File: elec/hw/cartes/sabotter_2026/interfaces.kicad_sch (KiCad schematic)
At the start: 43 parts, among them J10 2-1445055-3, J11 3-794618-6, J12 22053031, J13 3-794618-6, J6 794618-4, J7 A3C-16DA-2DSC71, J8 A3C-16DA-2DSC71, J9 794618-4, U6 TCAN1042DRQ1, U7 TCA6408ARGTR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

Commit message: switchs added to motor ribbon cable
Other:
- moved on the sheet: C27, D6, R51, R52, R53, R58, TP6, U7

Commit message: sabotter wip
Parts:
- removed J10: 2-1445055-3, cocotter_connectors:2-1445055-3, symbol cocotter_connectors:2-1445055-3
- removed J11: 3-794618-6, cocotter_connectors:3-794618-6, symbol cocotter_connectors:3-794618-6
- removed J12: 22053031, cocotter_connectors:22053031, symbol cocotter_connectors:22053031
- removed J7: A3C-16DA-2DSC71, cocotter_connectors:A3C-16DA-2DSC71, symbol cocotter_connectors:sabotter_to_unioc_pw
- removed J8: A3C-16DA-2DSC71, cocotter_connectors:A3C-16DA-2DSC71, symbol cocotter_connectors:sabotter_to_unioc_com
- removed R57: 91k 1%, cocotter_resistor:r0603_reflow, symbol cocotter_resistors:R_91k_0603_1%
- added C30: 100nF 50V, cocotter_capacitors:C_0603_1608Metric, symbol cocotter_capacitors:C_100nF_50V_0603
- added J10: 2-1445051-3, cocotter_connectors:2-1445051-3, symbol cocotter_connectors:2-1445051-3
- added J11: 22272051, cocotter_connectors:22272051, symbol cocotter_connectors:22272051
- added J12: 22272031, cocotter_connectors:22272031, symbol cocotter_connectors:22272031
- added J18: ~, cocotter_connectors:188275-4, symbol cocotter_connectors:unioc_uart
- added R58, R59, R60, R61: 0R, cocotter_resistor:r0603_reflow, symbol cocotter_resistors:R_0R_0603
- added R62, R63: 91k 1%, cocotter_resistor:r0603_reflow, symbol cocotter_resistors:R_91k_0603_1%
- added U9: ~, cocotter_ic:OLED_0.96inch, symbol cocotter_ic:OLED_0.96inch
- J13: value 3-794618-6 -> 3-794630-6; footprint cocotter_connectors:3-794618-6 -> cocotter_connectors:3-794630-6; symbol cocotter_connectors:3-794618-6 -> cocotter_connectors:3-794630-6
- J6, J9: value 794618-4 -> 3-794630-4; footprint cocotter_connectors:798618-4 -> cocotter_connectors:3-794630-4; symbol cocotter_connectors:794618-4 -> cocotter_connectors:3-794630-4
- renumbered R51 to R50, R50 to R51, R56 to R54, R54 to R55, R55 to R56, R58 to R57
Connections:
- net +3V3: now also J13.4, J11.4, R60.2, R61.2; no longer J13.2
- net +5V: now also J12.3
- net CAN_H: now also J10.3
- net CAN_L: now also J10.2
- net GND: now also C30.2, J10.1, J11.1, J12.1, J18.2 (GND), R58.1, R59.2, R62.2, R63.2
- net brake_mot_3v3: now also U7.7 (P4); no longer U7.9 (P6)
- net can_tx_3v3: now also U6.1 (TXD); no longer U6.3 (Vcc)
- net ctc_left_3v3: now also U7.8 (P5); no longer U7.5 (P3)
- net ctc_right_3v3: now also U7.9 (P6); no longer U7.4 (P2)
- net enable_tof_3v3: now also J13.5, U7.4 (P2), R63.1; no longer J13.4, U7.8 (P5)
- net reset_tof_3v3: now also U7.5 (P3), R62.1; no longer U7.7 (P4)
- net scl_3v3: now also J11.2, U9.3 (SCL)
- net scl_tof_3v3: now also J13.2; no longer J13.3
- net sda_3v3: now also J11.3, U9.4 (SDA)
- net sda_tof_3v3: now also J13.3; no longer J13.5
- net at D7.2 (DOUT): now also J12.2
- net at R54.2: now also J11.5
- net at R45.1: now also J18.1 (RX_from_out)
- net at R43.1: now also J18.4 (TX_from_out)
- new net: C30.1, R59.1, R60.1, U9.2 (VCC)
- new net: R58.2, R61.1, U9.1 (GND)
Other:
- note added: "HMI screen"
- moved on the sheet: R54

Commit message: sabotter wip
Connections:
- net brake_mot_3v3: now also U7.5 (P3); no longer U7.7 (P4)
- net color_select_3v3: now also U7.10 (P7); no longer U7.3 (P1)
- net ctc_left_3v3: now also U7.7 (P4); no longer U7.8 (P5)
- net ctc_right_3v3: now also U7.8 (P5); no longer U7.9 (P6)
- net enable_tof_3v3: now also U7.3 (P1); no longer U7.4 (P2)
- net led_com_3v3: now also U7.2 (P0); no longer U7.10 (P7)
- net reset_tof_3v3: now also U7.4 (P2); no longer U7.5 (P3)
- net scl_tof_3v3: now also J13.3; no longer J13.2
- net sda_tof_3v3: now also J13.2; no longer J13.3
- net starting_cord_3v3: now also U7.9 (P6); no longer U7.2 (P0)
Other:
- moved on the sheet: D6, R57, TP6

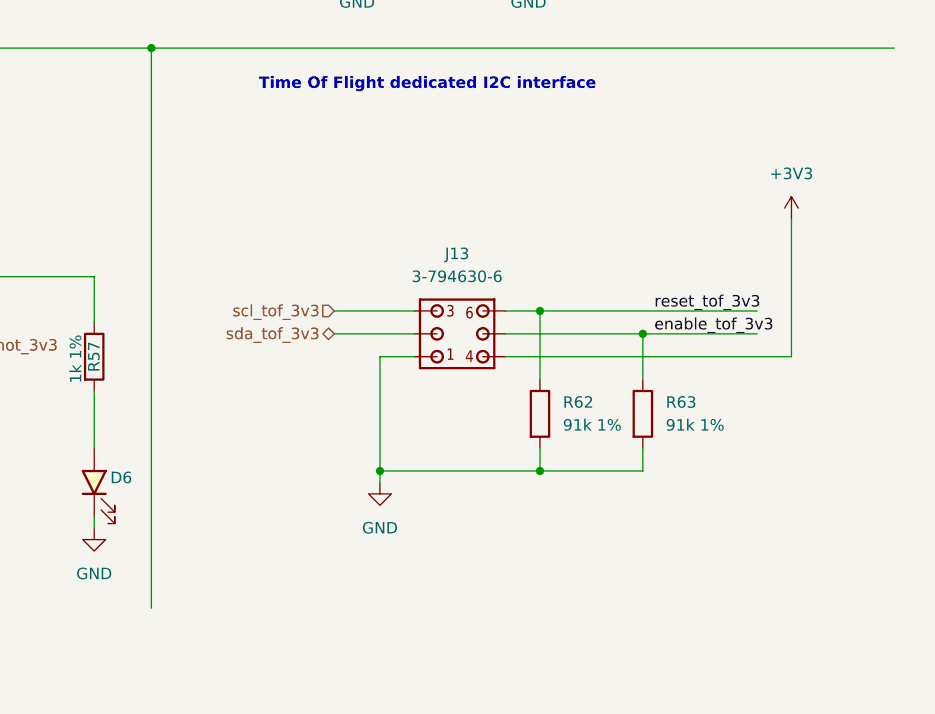
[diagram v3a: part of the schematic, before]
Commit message: tof irq added, needs routing
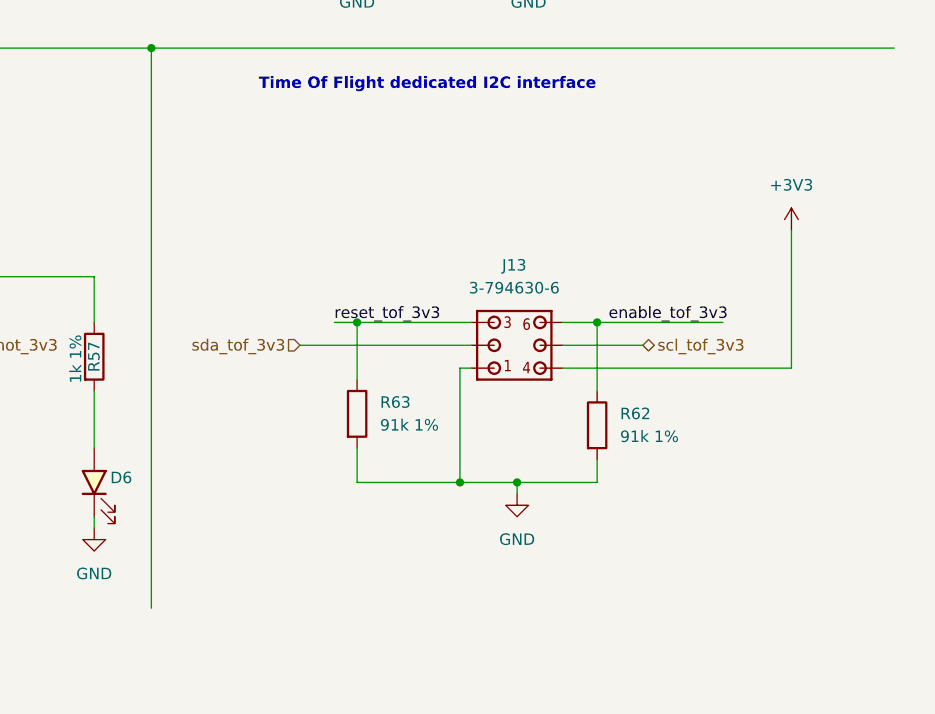
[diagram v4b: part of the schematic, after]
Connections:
- net enable_tof_3v3: now also J13.6, R62.1; no longer J13.5, R63.1
- net reset_tof_3v3: now also J13.3, R63.1; no longer J13.6, R62.1
- net scl_tof_3v3: now also J13.5; no longer J13.3
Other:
- moved on the sheet: J13, R62, R63

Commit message: sabotter corrections wip
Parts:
- added R65: 0R, cocotter_resistor:r0603_reflow, symbol cocotter_resistors:R_0R_0603
- added SW3: SLW-713515-2A-SMT-TR, cocotter_others:SLW-713515-2A-SMT-TR, symbol cocotter_connectors:SLW-713515-2A-SMT-TR
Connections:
- net GND: now also SW3.2
- net color_select_3v3: now also R65.2
- new net: R65.1, SW3.1
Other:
- moved on the sheet: C25, C26, C27, D6, J9, R49, R50, R51, R52, R53, R57, TP6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

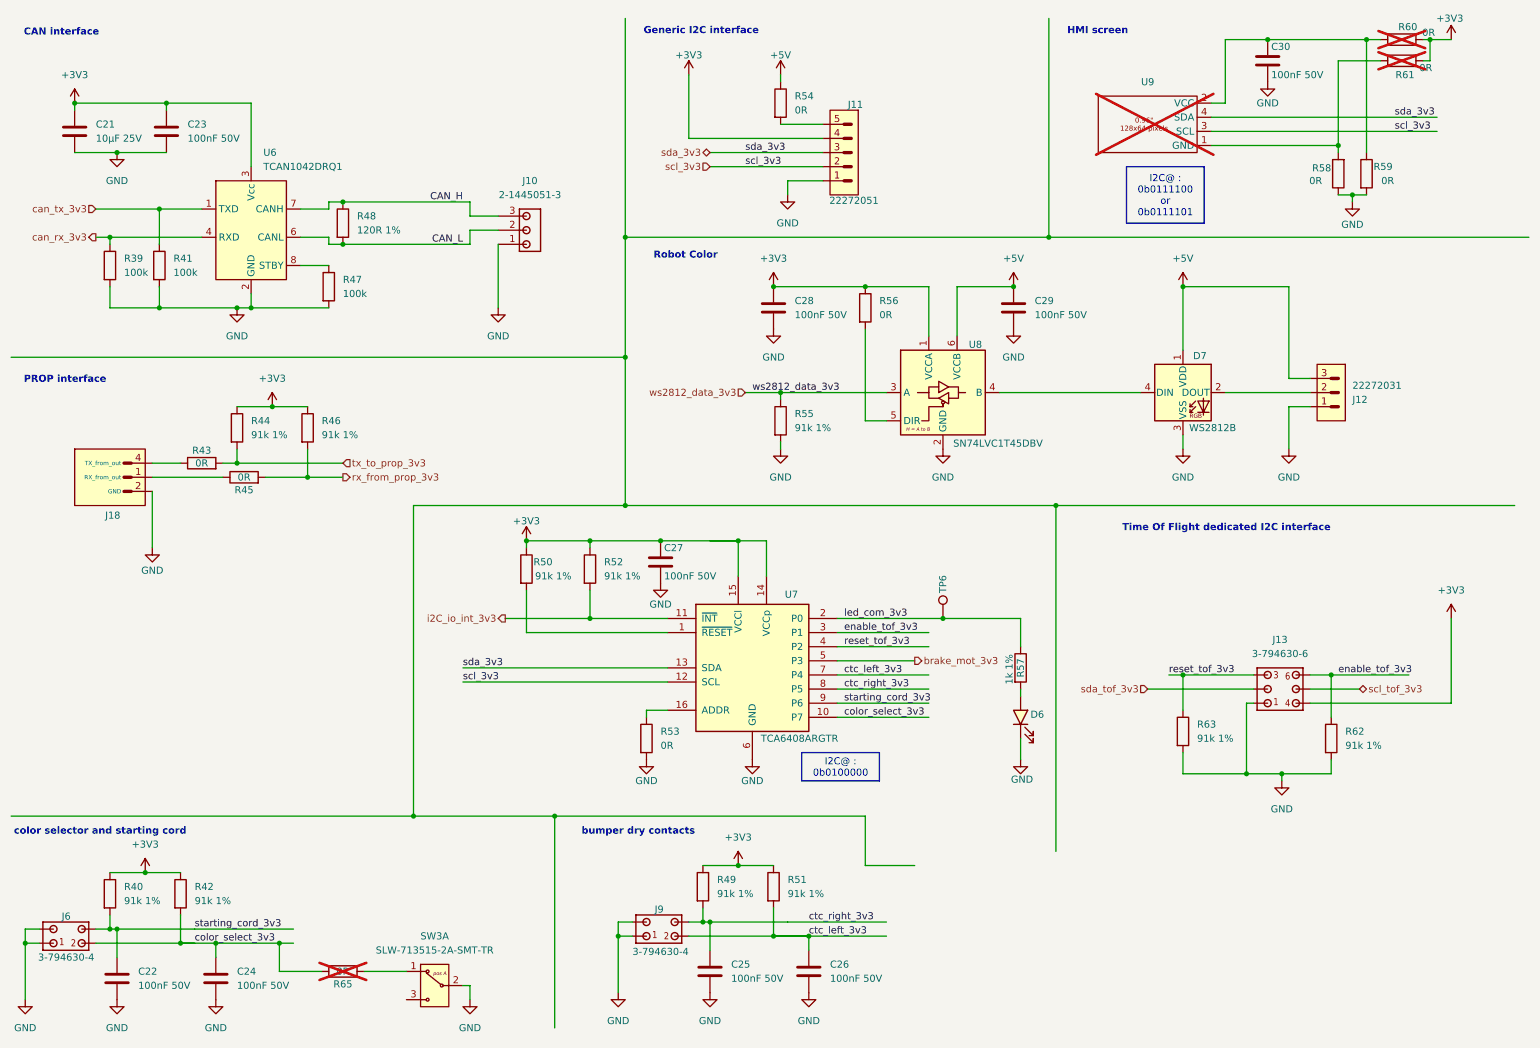
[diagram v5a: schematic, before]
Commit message: sabotter upodate : switch added to uc reset and color selection
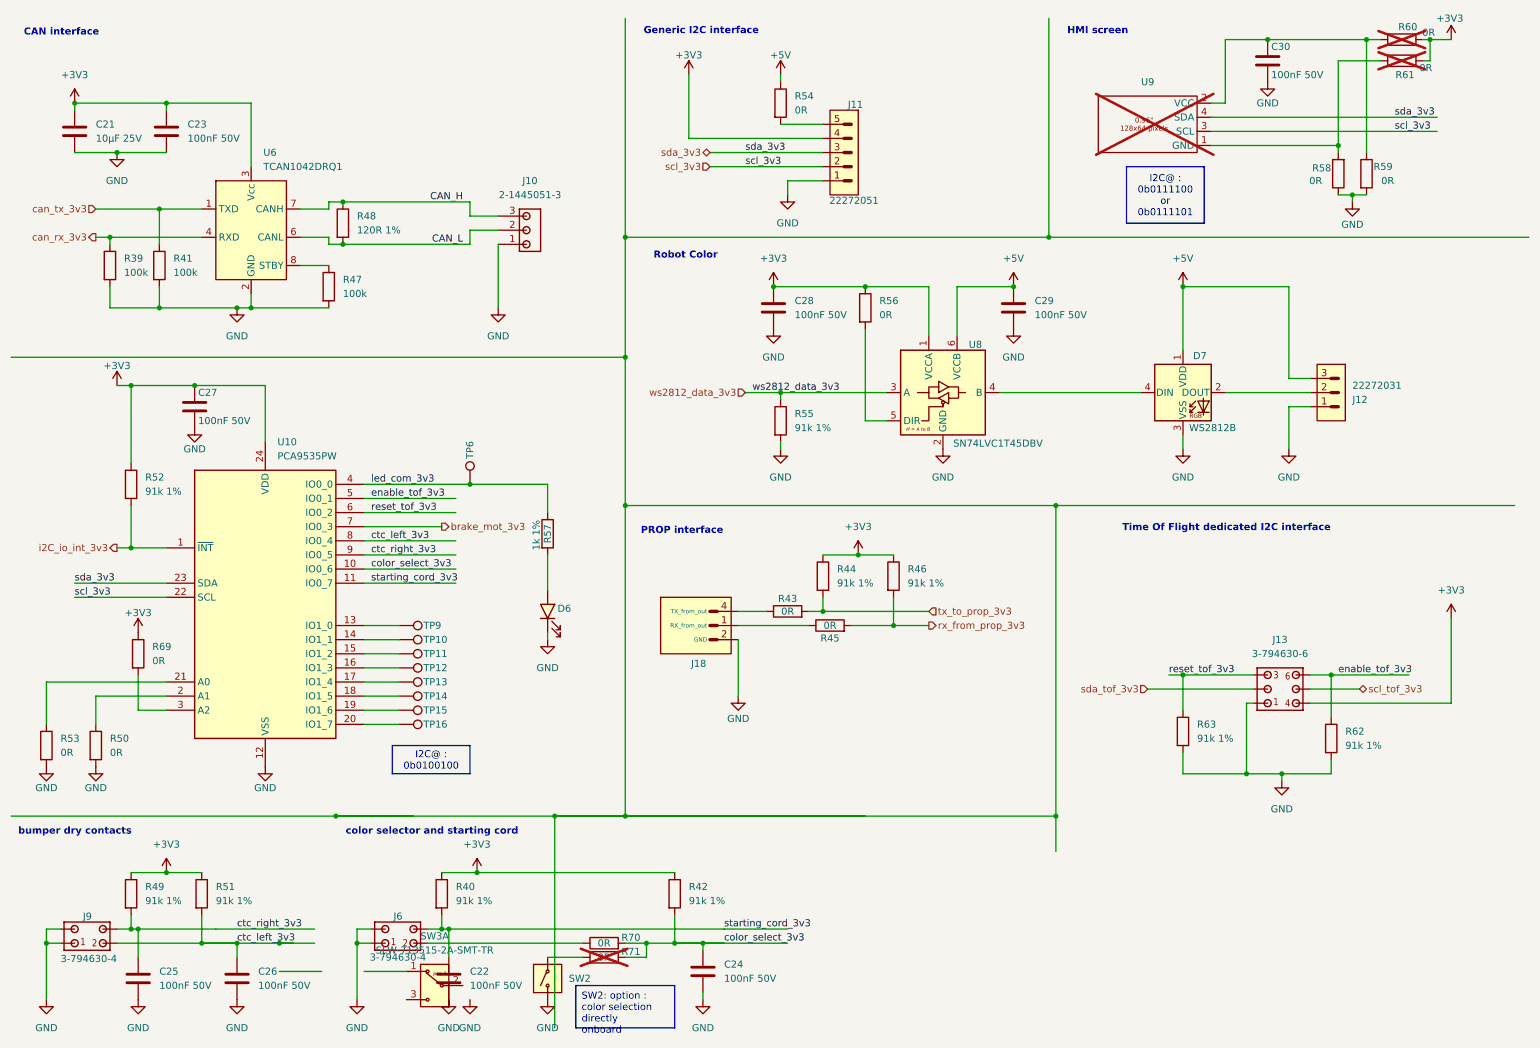
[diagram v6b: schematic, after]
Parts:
- removed R50: 91k 1%, cocotter_resistor:r0603_reflow, symbol cocotter_resistors:R_91k_0603_1%
- removed R65: 0R, cocotter_resistor:r0603_reflow, symbol cocotter_resistors:R_0R_0603
- removed U7: TCA6408ARGTR, cocotter_ic:VQFN-16-1EP_3x3mm_P0.5mm_EP1.1x1.1mm, symbol cocotter_ic:TCA6408ARGTR
- added R50, R69, R70, R71: 0R, cocotter_resistor:r0603_reflow, symbol cocotter_resistors:R_0R_0603
- added SW2: DSIC01LSGER, cocotter_others:DIP_SW_SMD-1P, symbol cocotter_others:DIP_SW_SMD-1P
- added TP10, TP11, TP12, TP13, TP14, TP15, TP16, TP9: TestPoint, cocotter_others:testpoint-THT-0.5mm, symbol cocotter_others:TestPoint
- added U10: PCA9535PW, Package_SO:TSSOP-24_4.4x7.8mm_P0.65mm, symbol cocotter_ic:PCA9535PW
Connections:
- net +3V3: now also R69.1, U10.24 (VDD)
- net GND: now also R50.2, SW2.1, U10.12 (VSS); no longer SW3.2
- net brake_mot_3v3: now also U10.7 (IO0_3)
- net color_select_3v3: now also R70.2, R71.2, U10.10 (IO0_6); no longer J6.2
- net ctc_left_3v3: now also U10.8 (IO0_4)
- net ctc_right_3v3: now also U10.9 (IO0_5)
- net enable_tof_3v3: now also U10.5 (IO0_1)
- net i2C_io_int_3v3: now also U10.1 (~{INT})
- net led_com_3v3: now also U10.4 (IO0_0)
- net reset_tof_3v3: now also U10.6 (IO0_2)
- net scl_3v3: now also U10.22 (SCL)
- net sda_3v3: now also U10.23 (SDA)
- net starting_cord_3v3: now also U10.11 (IO0_7)
- net at R53.1: now also U10.21 (A0)
- new net: R69.2, U10.3 (A2)
- new net: TP14.1, U10.18 (IO1_5)
- new net: TP11.1, U10.15 (IO1_2)
- new net: TP16.1, U10.20 (IO1_7)
- new net: R71.1, SW2.2
- new net: J6.2, R70.1
- new net: TP9.1, U10.13 (IO1_0)
- new net: TP10.1, U10.14 (IO1_1)
- new net: TP12.1, U10.16 (IO1_3)
- new net: TP13.1, U10.17 (IO1_4)
- new net: TP15.1, U10.19 (IO1_6)
- new net: R50.1, U10.2 (A1)
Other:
- moved on the sheet: C22, C24, C25, C26, C27, D6, J18, J6, J9, R40, R42, R43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

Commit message: sabotter corrected after review
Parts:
- removed SW3: SLW-713515-2A-SMT-TR, cocotter_others:SLW-713515-2A-SMT-TR, symbol cocotter_connectors:SLW-713515-2A-SMT-TR
- added R37: 0R, cocotter_resistor:r0603_reflow, symbol cocotter_resistors:R_0R_0603
- R40, R42, R44, R46, R49, R51, R52, R55, R62, R63: value 91k 1% -> 100k; symbol cocotter_resistors:R_91k_0603_1% -> cocotter_resistors:R_100k_0603_1%; JLCPCB Part # C23265 -> C25803; Specification 91k 0603 1% 100mW -> 100k 0603 1% 100mW; mouser (none) -> 603-RC0603FR-10100KL
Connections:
- net +5V: now also R37.2
- net i2C_io_int_3v3 renamed irq_io_3v3
- new net: J18.3 (NC), R37.1
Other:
- moved on the sheet: C22, C24, D6, J6, R40, R42, R57, R70, R71, SW2

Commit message: jlcpcb part added
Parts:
- D7: JLCPCB Part # (none) -> C2843785
- J10: JLCPCB Part # (none) -> C17473329
- J11: JLCPCB Part # (none) -> C585785
- J12: JLCPCB Part # (none) -> C471416
- J13: JLCPCB Part # (none) -> C305795
- J18: value ~ -> 188275-4; JLCPCB Part # (none) -> C720206
- J6, J9: JLCPCB Part # (none) -> C5164688
- U6: JLC C118837 -> (none); JLCPCB Part # (none) -> C118837
